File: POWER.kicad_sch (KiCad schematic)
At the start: 11 parts, among them U7 TPS560430XDBVR, U8 SPX3819M5-L-3-3/TR

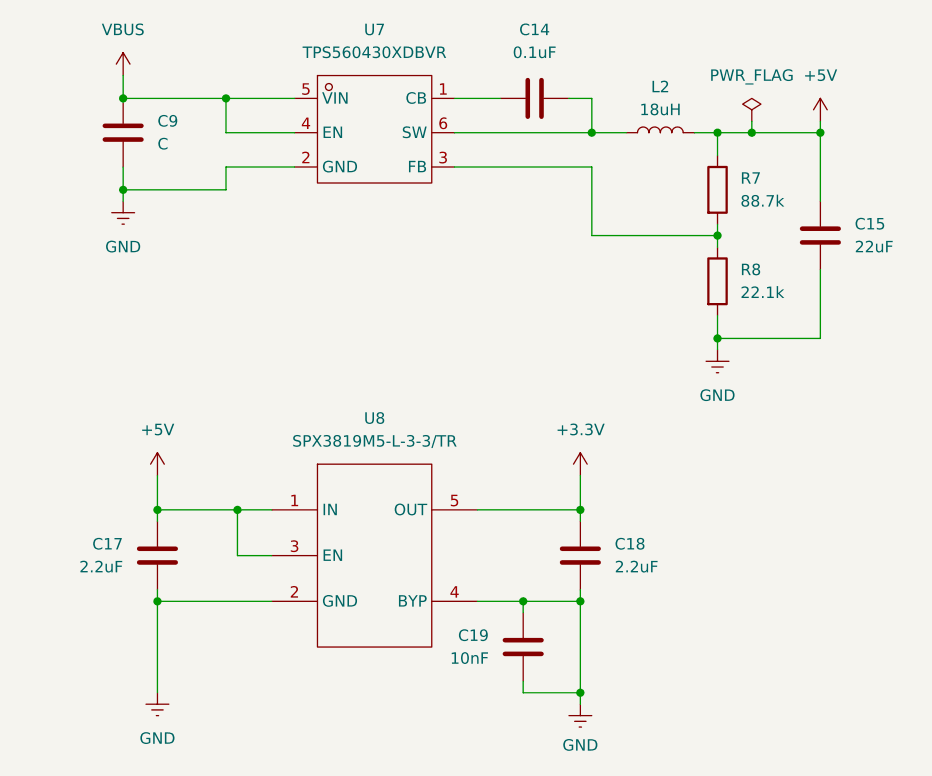
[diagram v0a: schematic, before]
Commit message: feat: add can and usart connector
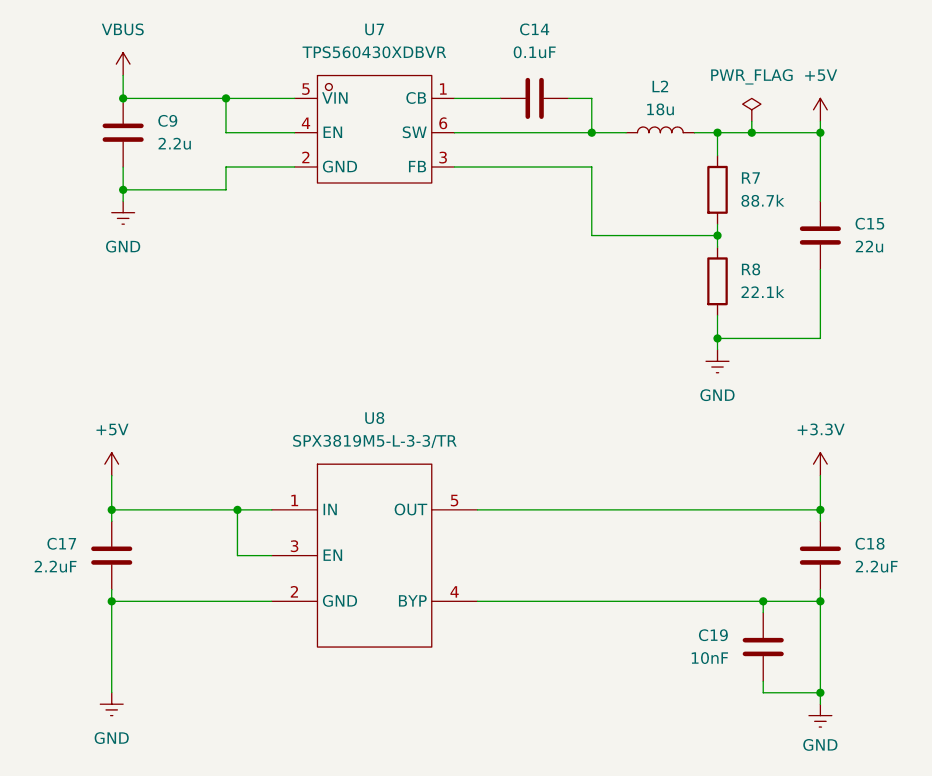
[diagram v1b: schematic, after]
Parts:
- C15: value 22uF -> 22u
- C9: value C -> 2.2u
- L2: value 18uH -> 18u
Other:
- moved on the sheet: C17, C18, C19

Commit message: change components
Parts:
- added CN1: XT30UPB-F30.G.Y, EasyEDA_Lib:CONN-TH_XT30UPB-F, symbol EasyEDA_Lib:XT30UPB-F
- added D4, D7: LED, symbol Device:LED
- added R13, R17: 1k, PCM_Resistor_SMD_AKL:R_0402_1005Metric, symbol Device:R
- C14: value 0.1uF -> 0.1u; footprint (none) -> Capacitor_SMD:C_0402_1005Metric
- C15, C9: footprint (none) -> Capacitor_SMD:C_0402_1005Metric
- C17, C18: value 2.2uF -> 2.2u; footprint (none) -> Capacitor_SMD:C_0402_1005Metric
- C19: value 10nF -> 10n; footprint (none) -> Capacitor_SMD:C_0402_1005Metric
- L2: footprint (none) -> EasyEDA_Lib:IND-SMD_L3.0-W3.0_FNR30XXS
- R7, R8: footprint (none) -> PCM_Resistor_SMD_AKL:R_0402_1005Metric
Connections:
- net +3.3V: now also D4.2 (A)
- net +5V: now also D7.2 (A)
- net GND: now also CN1.2 (-), R13.2, R17.2
- net VBUS renamed +24V
- net +24V: now also CN1.1 (+)
- new net: D7.1 (K), R17.1
- new net: D4.1 (K), R13.1
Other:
- note added: "24V to 5V Buck Convertor"
- note added: "5V to 3.3V LDO Regulator"
- note added: "max cont. current: 600mA frequency: 1.1Mhz"
- note added: "max current 950mA"
- moved on the sheet: C14, C15, C17, C18, C19, C9, L2, R7, R8, U7, U8

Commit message: update sch
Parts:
- D4, D7: footprint (none) -> LED_SMD:LED_0603_1608Metric
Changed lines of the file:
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@@
+	)
+	(junction
+		(at 71.12 68.58)
+		(diameter 0)
+		(color 0 0 0 0)
 	)
 	(junction
@@
 		(color 0 0 0 0)
 	)
+	(junction
+		(at 147.32 127)
+		(diameter 0)
+		(color 0 0 0 0)
+	)
 	(wire
 		(pts
@@
 	(wire
 		(pts
-			(xy 66.04 68.58) (xy 80.01 68.58)
+			(xy 66.04 68.58) (xy 71.12 68.58)
 		)
 		(stroke
@@
 	(wire
 		(pts
+			(xy 147.32 123.19) (xy 147.32 127)
+		)
+		(stroke
+			(width 0)
+			(type default)
+		)
+	)
+	(wire
+		(pts
 			(xy 129.54 58.42) (xy 132.08 58.42)
 		)
@@
 	(wire
 		(pts
+			(xy 71.12 68.58) (xy 71.12 69.85)
+		)
+		(stroke
+			(width 0)
+			(type default)
+		)
+	)
+	(wire
+		(pts
 			(xy 149.86 62.23) (xy 157.48 62.23)
 		)
@@
 	(wire
 		(pts
-			(xy 138.43 127) (xy 152.4 127)
+			(xy 138.43 127) (xy 147.32 127)
 		)
 		(stroke
@@
 	(wire
 		(pts
+			(xy 147.32 127) (xy 152.4 127)
+		)
+		(stroke
+			(width 0)
+			(type default)
+		)
+	)
+	(wire
+		(pts
 			(xy 157.48 60.96) (xy 157.48 62.23)
+		)
+		(stroke
+			(width 0)
+			(type default)
+		)
+	)
+	(wire
+		(pts
+			(xy 71.12 68.58) (xy 80.01 68.58)
 		)
 		(stroke
@@
 			)
 		)
-		(property "Footprint" ""
+		(property "Footprint" "LED_SMD:LED_0603_1608Metric"
 			(at 168.91 69.85 0)
 			(effects
@@
 	)
 	(symbol
+		(lib_id "power:PWR_FLAG")
+		(at 71.12 69.85 0)
+		(mirror x)
+		(unit 1)
+		(exclude_from_sim no)
+		(in_bom yes)
+		(on_board yes)
+		(dnp no)
+		(property "Reference" "#FLG06"
+			(at 71.12 71.755 0)
+			(effects
+				(font
+					(size 1.27 1.27)
+				)
+				(hide yes)
+			)
+		)
+		(property "Value" "PWR_FLAG"
+			(at 71.12 74.93 0)
+			(effects
+				(font
+					(size 1.27 1.27)
+				)
+			)
+		)
+		(property "Footprint" ""
+			(at 71.12 69.85 0)
+			(effects
+				(font
+					(size 1.27 1.27)
+				)
+				(hide yes)
+			)
+		)
+		(property "Datasheet" "~"
+			(at 71.12 69.85 0)
+			(effects
+				(font
+					(size 1.27 1.27)
+				)
+				(hide yes)
+			)
+		)
+		(property "Description" "Special symbol for telling ERC where power comes from"
+			(at 71.12 69.85 0)
+			(effects
+				(font
+					(size 1.27 1.27)
+				)
+				(hide yes)
+			)
+		)
+		(pin "1"
+		)
+		(instances
+			(project "foc-stepper-driver"
+				(path "/e8a1091a-f86c-4a0e-9f89-1944d2e62a64/14216783-423b-4483-89a5-cc1a98e45568"
+					(reference "#FLG06")
+					(unit 1)
+				)
+			)
+		)
+	)
+	(symbol
 		(lib_id "power:GNDREF")
 		(at 138.43 151.13 0)
@@
 	)
 	(symbol
+		(lib_id "power:PWR_FLAG")
+		(at 147.32 123.19 0)
+		(unit 1)
+		(exclude_from_sim no)
+		(in_bom yes)
+		(on_board yes)
+		(dnp no)
+		(fields_autoplaced yes)
+		(property "Reference" "#FLG05"
+			(at 147.32 121.285 0)
+			(effects
+				(font
+					(size 1.27 1.27)
+				)
+				(hide yes)
+			)
+		)
+		(property "Value" "PWR_FLAG"
+			(at 147.32 118.11 0)
+			(effects
+				(font
+					(size 1.27 1.27)
+				)
+			)
+		)
+		(property "Footprint" ""
+			(at 147.32 123.19 0)
+			(effects
+				(font
+					(size 1.27 1.27)
+				)
+				(hide yes)
+			)
+		)
+		(property "Datasheet" "~"
+			(at 147.32 123.19 0)
+			(effects
+				(font
+					(size 1.27 1.27)
+				)
+				(hide yes)
+			)
+		)
+		(property "Description" "Special symbol for telling ERC where power comes from"
+			(at 147.32 123.19 0)
+			(effects
+				(font
+					(size 1.27 1.27)
+				)
+				(hide yes)
+			)
+		)
+		(pin "1"
+		)
+		(instances
+			(project "foc-stepper-driver"
+				(path "/e8a1091a-f86c-4a0e-9f89-1944d2e62a64/14216783-423b-4483-89a5-cc1a98e45568"
+					(reference "#FLG05")
+					(unit 1)
+				)
+			)
+		)
+	)
+	(symbol
 		(lib_id "power:+24V")
 		(at 80.01 55.88 0)
@@
 			)
 		)
-		(property "Footprint" ""
+		(property "Footprint" "LED_SMD:LED_0603_1608Metric"
 			(at 152.4 134.62 0)
 			(effects
